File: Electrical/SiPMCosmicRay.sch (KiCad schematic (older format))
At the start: 3 parts

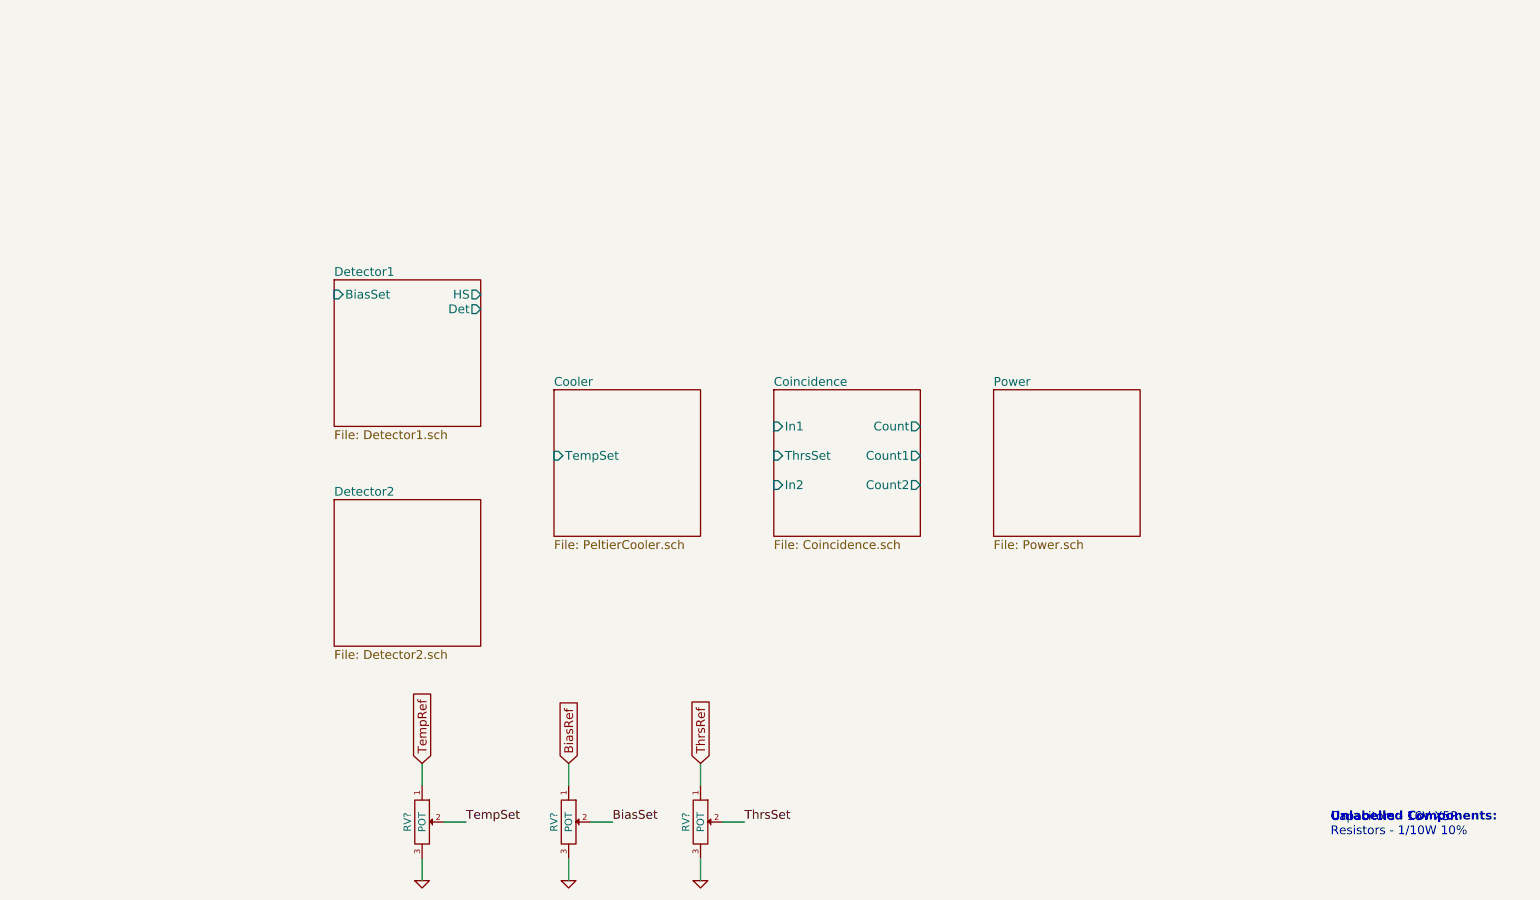
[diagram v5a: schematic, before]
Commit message: Added sensors/data logger with ChipKit Max
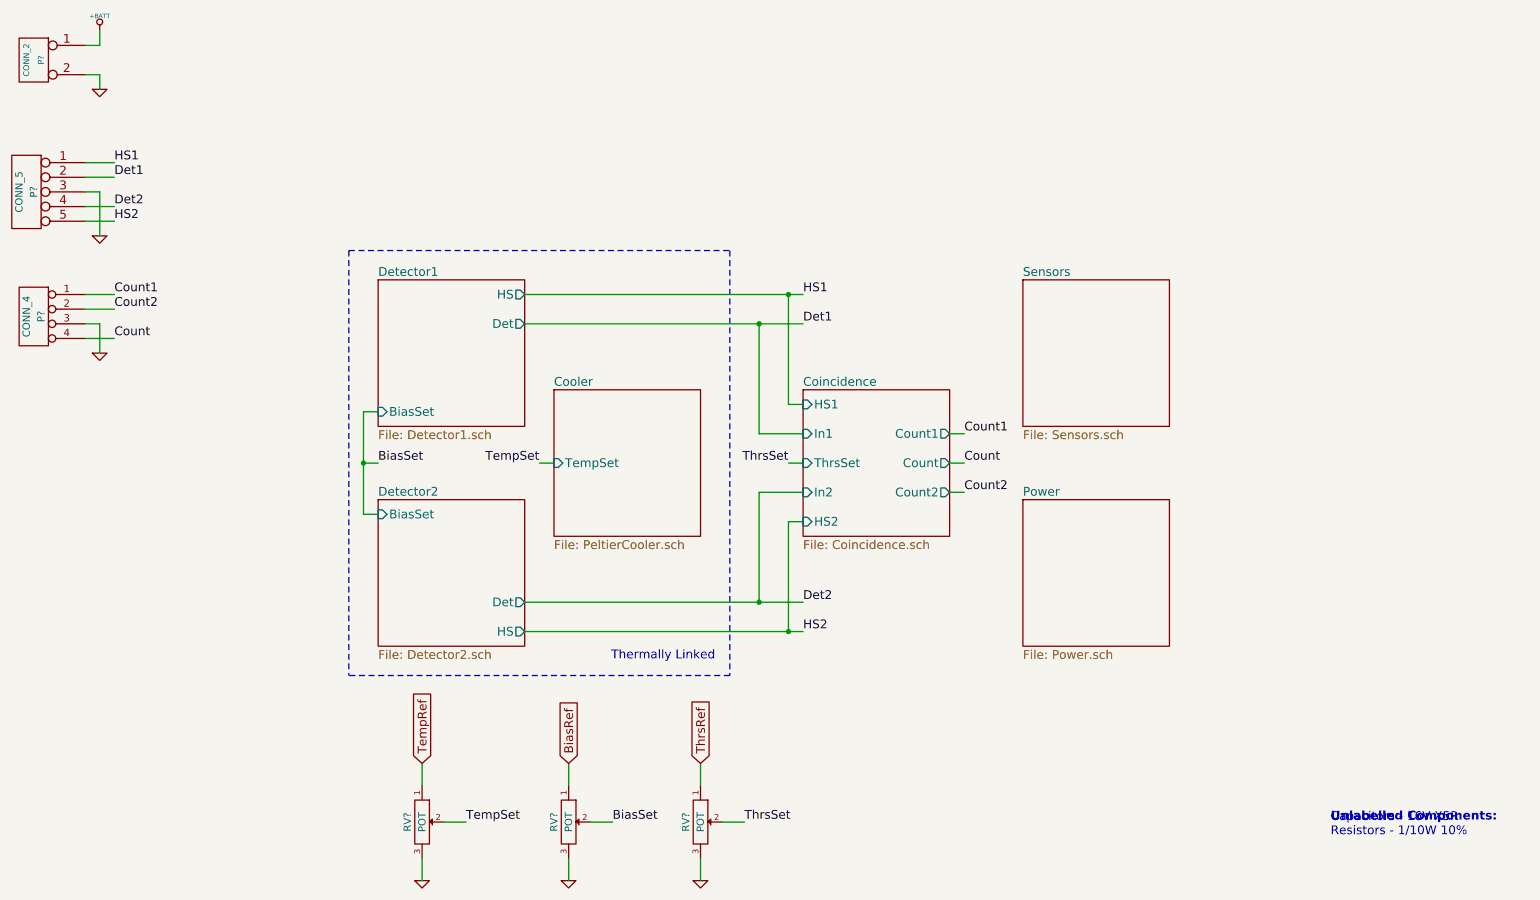
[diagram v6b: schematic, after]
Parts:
- added P?: CONN_2, symbol CONN_2
- added P?: CONN_5, symbol CONN_5
- added P?: CONN_4, symbol CONN_4
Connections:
- net GND: now also P?.2 (PM), P?.3, P?.3 (P3)
- new net +BATT: P?.1 (P1)
- new net Count: P?.4 (P4)
- new net Count1: P?.1 (P1)
- new net Count2: P?.2 (P2)
- new net Det1: P?.2
- new net Det2: P?.4
- new net HS1: P?.1
- new net HS2: P?.5
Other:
- note added: "Thermally Linked"
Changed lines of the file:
@@
-EESchema Schematic File Version 2  date 4/19/2013 7:14:36 PM
+EESchema Schematic File Version 2  date 5/4/2013 6:32:29 PM
 LIBS:power
 LIBS:device
@@
 $Descr A4 11700 8267
 encoding utf-8
-Sheet 1 6
+Sheet 1 7
 Title "Cosmic Ray Detector"
-Date "20 apr 2013"
+Date "4 may 2013"
 Rev "1A"
 Comp "Ethan Harstad"
@@
 Comment4 ""
 $EndDescr
+Wire Wire Line
+	1500 3200 1500 3000
+Wire Wire Line
+	1500 3000 1400 3000
+Wire Wire Line
+	7400 3950 7300 3950
+Wire Wire Line
+	7400 4150 7300 4150
+Wire Wire Line
+	1600 2000 1400 2000
+Wire Wire Line
+	1600 1900 1400 1900
+Connection ~ 6200 5100
+Wire Wire Line
+	6300 5100 4400 5100
+Connection ~ 6000 3000
+Wire Wire Line
+	6300 3000 4400 3000
+Wire Wire Line
+	1500 1000 1500 1100
+Wire Wire Line
+	1500 1100 1400 1100
+Wire Wire Line
+	6300 4350 6200 4350
+Wire Wire Line
+	6200 4350 6200 5100
+Wire Wire Line
+	6300 3550 6200 3550
+Wire Wire Line
+	6200 3550 6200 2800
+Wire Wire Line
+	6200 3950 6300 3950
+Wire Notes Line
+	3200 2500 3200 5400
+Wire Notes Line
+	3200 2500 5800 2500
+Wire Notes Line
+	5800 2500 5800 5400
+Wire Notes Line
+	5800 5400 3200 5400
+Wire Wire Line
+	4500 3950 4600 3950
+Wire Wire Line
+	4700 6000 4700 6150
+Wire Wire Line
+	5600 6650 5600 6800
+Wire Wire Line
+	5900 6400 5750 6400
+Wire Wire Line
+	4000 6400 3850 6400
+Wire Wire Line
+	3700 6800 3700 6650
+Wire Wire Line
+	5000 6400 4850 6400
+Wire Wire Line
+	4700 6800 4700 6650
+Wire Wire Line
+	3700 6000 3700 6150
+Wire Wire Line
+	5600 6000 5600 6150
+Wire Wire Line
+	3300 3950 3400 3950
+Wire Wire Line
+	3400 3600 3300 3600
+Wire Wire Line
+	3300 3600 3300 4300
+Wire Wire Line
+	3300 4300 3400 4300
+Connection ~ 3300 3950
+Wire Wire Line
+	6000 3000 6000 3750
+Wire Wire Line
+	6000 3750 6300 3750
+Wire Wire Line
+	6000 4900 6000 4150
+Wire Wire Line
+	6000 4150 6300 4150
+Wire Wire Line
+	1500 1400 1500 1300
+Wire Wire Line
+	1500 1300 1400 1300
+Wire Wire Line
+	6300 2800 4400 2800
+Connection ~ 6200 2800
+Wire Wire Line
+	6300 4900 4400 4900
+Connection ~ 6000 4900
+Wire Wire Line
+	1500 2400 1500 2100
+Wire Wire Line
+	1500 2100 1400 2100
+Wire Wire Line
+	1600 2200 1400 2200
+Wire Wire Line
+	1600 2300 1400 2300
+Wire Wire Line
+	7300 3750 7400 3750
+Wire Wire Line
+	1400 2800 1600 2800
+Wire Wire Line
+	1400 2900 1600 2900
+Wire Wire Line
+	1400 3100 1600 3100
+$Comp
+L GND #PWR?
+U 1 1 518591FF
+P 1500 3200
+F 0 "#PWR?" H 1500 3200 30  0001 C CNN
+F 1 "GND" H 1500 3130 30  0001 C CNN
+	1    1500 3200
+	1    0    0    -1
+$EndComp
+Text Label 1600 3100 0    60   ~ 0
+Count
+Text Label 1600 2900 0    60   ~ 0
+Count2
+Text Label 1600 2800 0    60   ~ 0
+Count1
+Text Label 7400 3950 0    60   ~ 0
+Count
+Text Label 7400 4150 0    60   ~ 0
+Count2
+Text Label 7400 3750 0    60   ~ 0
+Count1
+$Comp
+L CONN_4 P?
+U 1 1 51859177
+P 1050 2950
+F 0 "P?" V 1000 2950 50  0000 C CNN
+F 1 "CONN_4" V 1100 2950 50  0000 C CNN
+	1    1050 2950
+	-1   0    0    -1
+$EndComp
+$Comp
+L CONN_5 P?
+U 1 1 518590D3
+P 1000 2100
+F 0 "P?" V 950 2100 50  0000 C CNN
+F 1 "CONN_5" V 1050 2100 50  0000 C CNN
+	1    1000 2100
+	-1   0    0    -1
+$EndComp
+$Comp
+L GND #PWR?
+U 1 1 5185902C
+P 1500 2400
+F 0 "#PWR?" H 1500 2400 30  0001 C CNN
+F 1 "GND" H 1500 2330 30  0001 C CNN
+	1    1500 2400
+	1    0    0    -1
+$EndComp
+Text Label 1600 2200 0    60   ~ 0
+Det2
+Text Label 1600 2000 0    60   ~ 0
+Det1
+Text Label 1600 2300 0    60   ~ 0
+HS2
+Text Label 1600 1900 0    60   ~ 0
+HS1
+Text Label 6300 5100 0    60   ~ 0
+HS2
+Text Label 6300 4900 0    60   ~ 0
+Det2
+Text Label 6300 3000 0    60   ~ 0
+Det1
+Text Label 6300 2800 0    60   ~ 0
+HS1
+$Comp
+L GND #PWR?
+U 1 1 51858EC7
+P 1500 1400
+F 0 "#PWR?" H 1500 1400 30  0001 C CNN
+F 1 "GND" H 1500 1330 30  0001 C CNN
+	1    1500 1400
+	1    0    0    -1
+$EndComp
+$Comp
+L +BATT #PWR?
+U 1 1 51858EC2
+P 1500 1000
+F 0 "#PWR?" H 1500 950 20  0001 C CNN
+F 1 "+BATT" H 1500 1100 30  0000 C CNN
+	1    1500 1000
+	1    0    0    -1
+$EndComp
+$Comp
+L CONN_2 P?
+U 1 1 51858EB7
+P 1050 1200
+F 0 "P?" V 1000 1200 40  0000 C CNN
+F 1 "CONN_2" V 1100 1200 40  0000 C CNN
+	1    1050 1200
+	-1   0    0    -1
+$EndComp
+$Sheet
+S 7800 2700 1000 1000
+U 51856772
+F0 "Sensors" 60
+F1 "Sensors.sch" 60
+$EndSheet
+Text Label 6200 3950 2    60   ~ 0
+ThrsSet
+$Sheet
+S 7800 4200 1000 1000
+U 516B8E64
+F0 "Power" 60
+F1 "Power.sch" 60
+$EndSheet
+Text Notes 5700 5300 2    60   ~ 0
+Thermally Linked
+Text Label 3400 3950 0    60   ~ 0
+BiasSet
+Text Label 4500 3950 2    60   ~ 0
+TempSet
+$Sheet
+S 3400 2700 1000 1000
+U 516B74CB
+F0 "Detector1" 60
+F1 "Detector1.sch" 60
+F2 "HS" O R 4400 2800 60
+F3 "Det" O R 4400 3000 60
+F4 "BiasSet" I L 3400 3600 60
+$EndSheet
 Text GLabel 3700 6000 1    60   Input ~ 0
 TempRef
-Wire Wire Line
-	5600 6000 5600 6150
-Wire Wire Line
-	3700 6000 3700 6150
-Wire Wire Line
-	4700 6800 4700 6650
-Wire Wire Line
-	5000 6400 4850 6400
-Wire Wire Line
-	3700 6800 3700 6650
-Wire Wire Line
-	4000 6400 3850 6400
-Wire Wire Line
-	5900 6400 5750 6400
-Wire Wire Line
-	5600 6650 5600 6800
-Wire Wire Line
-	4700 6000 4700 6150
 Text GLabel 5600 6000 1    60   Input ~ 0
 ThrsRef
@@
 $EndComp
 $Sheet
-S 6100 3450 1000 1000
+S 6300 3450 1000 1000
 U 516F2FCF
 F0 "Coincidence" 60
 F1 "Coincidence.sch" 60
-F2 "ThrsSet" I L 6100 3900 60
-F3 "In2" I L 6100 4100 60
-F4 "In1" I L 6100 3700 60
-F5 "Count" O R 7100 3700 60
-F6 "Count2" O R 7100 4100 60
-F7 "Count1" O R 7100 3900 60
-$EndSheet
-$Sheet
-S 7600 3450 1000 1000
-U 516B8E64
-F0 "Power" 60
-F1 "Power.sch" 60
-$EndSheet
-$Sheet
-S 3100 4200 1000 1000
+F2 "ThrsSet" I L 6300 3950 60
+F3 "In2" I L 6300 4150 60
+F4 "In1" I L 6300 3750 60
+F5 "Count" O R 7300 3950 60
+F6 "Count2" O R 7300 4150 60
+F7 "Count1" O R 7300 3750 60
+F8 "HS2" I L 6300 4350 60
+F9 "HS1" I L 6300 3550 60
+$EndSheet
+$Sheet
+S 3400 4200 1000 1000
 U 516B8E0E
 F0 "Detector2" 60
 F1 "Detector2.sch" 60
-$EndSheet
-$Sheet
-S 3100 2700 1000 1000
-U 516B74CB
-F0 "Detector1" 60
-F1 "Detector1.sch" 60
-F2 "HS" O R 4100 2800 60
-F3 "Det" O R 4100 2900 60
-F4 "BiasSet" I L 3100 2800 60
+F2 "Det" O R 4400 4900 60
+F3 "HS" O R 4400 5100 60
+F4 "BiasSet" I L 3400 4300 60
 $EndSheet
 $Sheet
@@
 F0 "Cooler" 60
 F1 "PeltierCooler.sch" 60
-F2 "TempSet" I L 4600 3900 60
+F2 "TempSet" I L 4600 3950 60
 $EndSheet
 Text Notes 9900 6400 0    60   ~ 12

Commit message: Annotated schematic
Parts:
- gave numbers to parts that had none: 6
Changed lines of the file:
@@
-EESchema Schematic File Version 2  date 5/4/2013 6:32:29 PM
+EESchema Schematic File Version 2  date 5/5/2013 3:54:39 PM
 LIBS:power
 LIBS:device
@@
 Sheet 1 7
 Title "Cosmic Ray Detector"
-Date "4 may 2013"
+Date "5 may 2013"
 Rev "1A"
 Comp "Ethan Harstad"
@@
 	1400 3100 1600 3100
 $Comp
-L GND #PWR?
+L GND #PWR4
 U 1 1 518591FF
 P 1500 3200
-F 0 "#PWR?" H 1500 3200 30  0001 C CNN
+F 0 "#PWR4" H 1500 3200 30  0001 C CNN
 F 1 "GND" H 1500 3130 30  0001 C CNN
 	1    1500 3200
@@
 Count1
 $Comp
-L CONN_4 P?
+L CONN_4 P3
 U 1 1 51859177
 P 1050 2950
-F 0 "P?" V 1000 2950 50  0000 C CNN
+F 0 "P3" V 1000 2950 50  0000 C CNN
 F 1 "CONN_4" V 1100 2950 50  0000 C CNN
 	1    1050 2950
@@
 $EndComp
 $Comp
-L CONN_5 P?
+L CONN_5 P1
 U 1 1 518590D3
 P 1000 2100
-F 0 "P?" V 950 2100 50  0000 C CNN
+F 0 "P1" V 950 2100 50  0000 C CNN
 F 1 "CONN_5" V 1050 2100 50  0000 C CNN
 	1    1000 2100
@@
 $EndComp
 $Comp
-L GND #PWR?
+L GND #PWR3
 U 1 1 5185902C
 P 1500 2400
-F 0 "#PWR?" H 1500 2400 30  0001 C CNN
+F 0 "#PWR3" H 1500 2400 30  0001 C CNN
 F 1 "GND" H 1500 2330 30  0001 C CNN
 	1    1500 2400
@@
 HS1
 $Comp
-L GND #PWR?
+L GND #PWR2
 U 1 1 51858EC7
 P 1500 1400
-F 0 "#PWR?" H 1500 1400 30  0001 C CNN
+F 0 "#PWR2" H 1500 1400 30  0001 C CNN
 F 1 "GND" H 1500 1330 30  0001 C CNN
 	1    1500 1400
@@
 $EndComp
 $Comp
-L +BATT #PWR?
+L +BATT #PWR1
 U 1 1 51858EC2
 P 1500 1000
-F 0 "#PWR?" H 1500 950 20  0001 C CNN
+F 0 "#PWR1" H 1500 950 20  0001 C CNN
 F 1 "+BATT" H 1500 1100 30  0000 C CNN
 	1    1500 1000
@@
 $EndComp
 $Comp
-L CONN_2 P?
+L CONN_2 P2
 U 1 1 51858EB7
 P 1050 1200
-F 0 "P?" V 1000 1200 40  0000 C CNN
+F 0 "P2" V 1000 1200 40  0000 C CNN
 F 1 "CONN_2" V 1100 1200 40  0000 C CNN
 	1    1050 1200
@@
 BiasRef
 $Comp
-L GND #PWR?
+L GND #PWR6
 U 1 1 51707B27
 P 4700 6800
-F 0 "#PWR?" H 4700 6800 30  0001 C CNN
+F 0 "#PWR6" H 4700 6800 30  0001 C CNN
 F 1 "GND" H 4700 6730 30  0001 C CNN
 	1    4700 6800
@@
 $EndComp
 $Comp
-L GND #PWR?
+L GND #PWR7
 U 1 1 51707B22
 P 5600 6800
-F 0 "#PWR?" H 5600 6800 30  0001 C CNN
+F 0 "#PWR7" H 5600 6800 30  0001 C CNN
 F 1 "GND" H 5600 6730 30  0001 C CNN
 	1    5600 6800
@@
 ThrsSet
 $Comp
-L POT RV?
+L POT RV3
 U 1 1 51707B04
 P 5600 6400
-F 0 "RV?" H 5600 6300 50  0000 C CNN
+F 0 "RV3" H 5600 6300 50  0000 C CNN
 F 1 "POT" H 5600 6400 50  0000 C CNN
 	1    5600 6400
@@
 BiasSet
 $Comp
-L POT RV?
+L POT RV2
 U 1 1 51707AEB
 P 4700 6400
-F 0 "RV?" H 4700 6300 50  0000 C CNN
+F 0 "RV2" H 4700 6300 50  0000 C CNN
 F 1 "POT" H 4700 6400 50  0000 C CNN
 	1    4700 6400
@@
 TempSet
 $Comp
-L GND #PWR?
+L GND #PWR5
 U 1 1 51707A98
 P 3700 6800
-F 0 "#PWR?" H 3700 6800 30  0001 C CNN
+F 0 "#PWR5" H 3700 6800 30  0001 C CNN
 F 1 "GND" H 3700 6730 30  0001 C CNN
 	1    3700 6800
@@
 $EndComp
 $Comp
-L POT RV?
+L POT RV1
 U 1 1 51707A88
 P 3700 6400
-F 0 "RV?" H 3700 6300 50  0000 C CNN
+F 0 "RV1" H 3700 6300 50  0000 C CNN
 F 1 "POT" H 3700 6400 50  0000 C CNN
 	1    3700 6400
